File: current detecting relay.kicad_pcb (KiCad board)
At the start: 2 copper layers, 13 x 20.5 mm, 18 parts, among them J30 197054003, J85 197054101, J86 197054101, J87 197054003, Q1 SPP18P06P H, U1 INA300, U2 ULN2001D, U3 ADP7182AUJZ-5.0

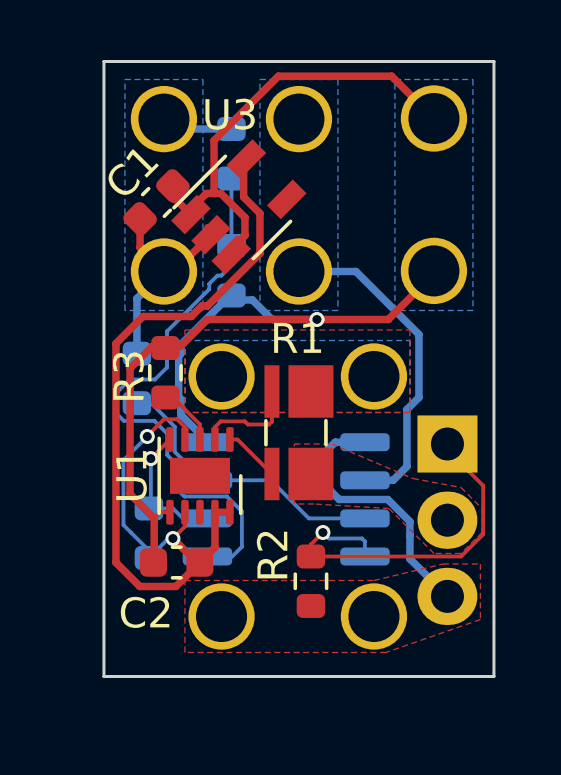
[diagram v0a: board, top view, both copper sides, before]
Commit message: Selected smaller transistors, layout tentative
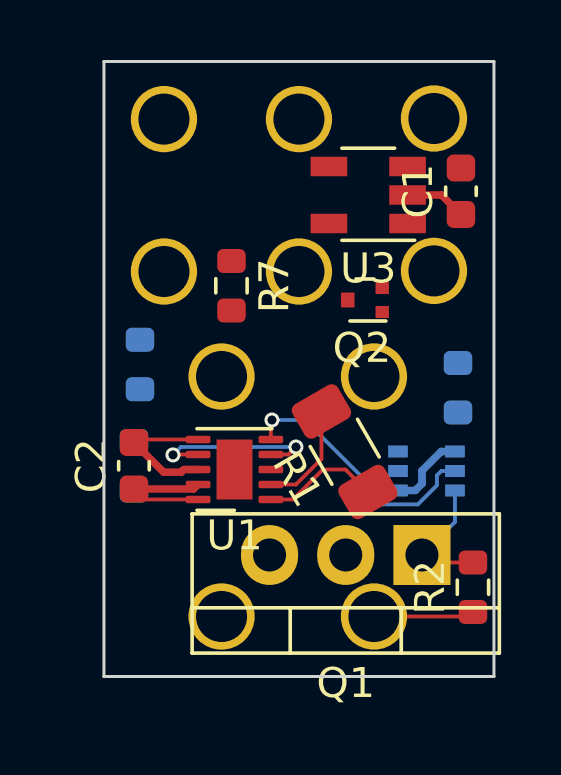
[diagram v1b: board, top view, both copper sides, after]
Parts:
- removed R6: 10K, Resistor_SMD:R_0603_1608Metric
- removed U2: ULN2001D, Package_SO:SOP-8_3.9x4.9mm_P1.27mm
- added Q2: Q_NPN_BEC, Package_TO_SOT_SMD:SOT-723, F.Cu at (108.7, 58.0)
- added Q3: BC846BDW1, Package_TO_SOT_SMD:SOT-363_SC-70-6, B.Cu at (110.8, 63.6)
- R1: footprint Resistor_SMD:R_Shunt_Ohmite_LVK12 -> Resistor_SMD:R_1206_3216Metric_Pad1.30x1.75mm_HandSolder
- R3: moved to B.Cu
- R7: moved to F.Cu
- moved R4 11.4 mm to (111.8, 60.9), turned to 270 degrees
- moved C1 10.2 mm to (111.9, 54.3), turned to 90 degrees
- moved R5 7.66 mm to (101.2, 60.1)
- moved R2 5.40 mm to (112.3, 67.5)
- moved R7 4.41 mm to (104.2, 57.5)
- moved U3 4.33 mm to (108.8, 54.5), turned to 180 degrees
- moved Q1 3.80 mm to (110.6, 66.5), turned to 180 degrees
- moved C2 3.53 mm to (101.0, 63.5), turned to 90 degrees
- moved R3 3.27 mm to (101.0, 63.5)
- moved R1 1.74 mm to (108.0, 63.0), turned to 120 degrees
- moved U1 1.17 mm to (104.3, 63.6), turned to 180 degrees
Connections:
- net Net-(R3-Pad2) renamed /LimSet
- J87 pad 1_1: /Vout -> /SHUNT-
- J87 pad 1_2: /Vout -> /SHUNT-
- R1 pad 2: /Vsense+ -> /SHUNT-
- U1 pad 1: /Vsense+ -> /SHUNT+
- U1 pad 2: /Vsense- -> /SHUNT-
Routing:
- net GND: track 43.6 -> 7.46 mm, vias 1 -> 0
- net /5V: track 32.8 -> 10.5 mm
- net Net-(Q3-Pad5): track 18.8 -> 0.00 mm
- net /LAMP: track 11.0 -> 0.00 mm
- net Net-(Q2-Pad1): track 9.68 -> 0.00 mm
- net /OutEnable: track 12.5 -> 4.41 mm, vias 1 -> 0
- net /SWin: track 9.74 -> 2.05 mm
- net /Vin: track 8.97 -> 3.36 mm
- net /ALERT: track 4.68 -> 8.73 mm
- net /SHUNT+: track 0.19 -> 3.96 mm
- net /SHUNT-: track 0.00 -> 3.62 mm
- net /Vsense-: track 3.48 -> 0.00 mm
- net /LimSet: track 2.32 -> 0.00 mm
- net /Vsense+: track 1.88 -> 0.00 mm
- removed copper zone on B.Cu, net /LAMP
- removed copper zone on F.Cu, net /SHUNT+
- removed copper zone on B.Cu, net /SWin
- removed copper zone on F.Cu, net /Vin
- removed copper zone on B.Cu, net /Vout
- removed copper zone on F.Cu, net /Vout
- removed copper zone on B.Cu, net GND

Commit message: Worked on layout and cleaning up silk screen
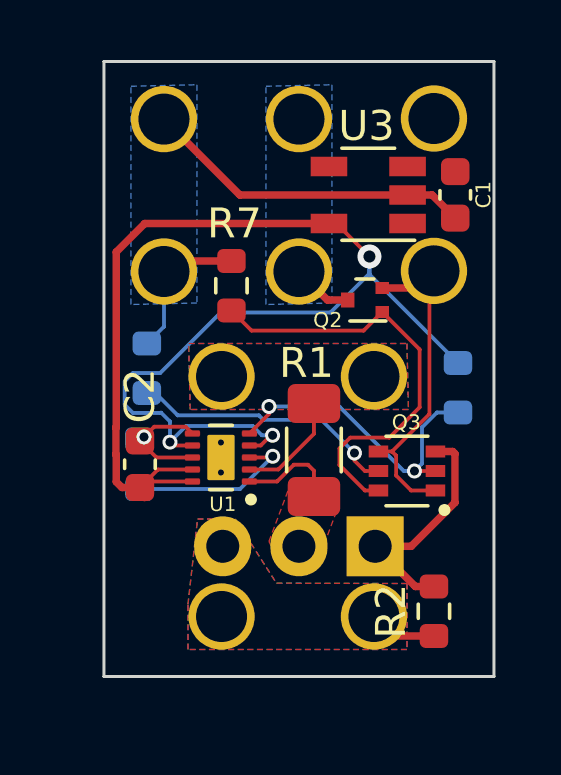
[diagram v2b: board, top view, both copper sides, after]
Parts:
- J30, J85, J86, J87, Ja87: moved to B.Cu
- Q3: moved to F.Cu
- U1: footprint Package_SON:WSON-10-1EP_2.5x2.5mm_P0.5mm_EP1.2x2mm -> footprints:SON40P200X200X80-11N
- moved Q1 1.59 mm to (109.0, 66.2)
- moved R2 1.53 mm to (111.0, 68.3)
- moved R1 1.03 mm to (107.0, 63.0), turned to 90 degrees
- moved Q3 0.65 mm to (110.1, 63.6)
- moved U1 0.60 mm to (103.9, 63.2)
- moved R5 0.26 mm to (101.4, 60.2)
- moved C1 0.22 mm to (111.7, 54.4)
- moved C2 0.21 mm to (101.2, 63.4)
- moved R3 0.19 mm to (101.2, 63.4)
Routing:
- net /5V: track 10.5 -> 45.9 mm, vias 2 -> 3
- net Net-(Q2-Pad1): track 0.00 -> 14.7 mm
- net /SWin: track 2.05 -> 15.9 mm
- net Net-(Q3-Pad5): track 0.00 -> 8.73 mm, vias 0 -> 1
- net GND: track 7.46 -> 15.6 mm, vias 0 -> 1
- net /LimSet: track 0.00 -> 5.69 mm, vias 0 -> 1
- net /OutEnable: track 4.41 -> 8.09 mm
- net /ALERT: track 8.73 -> 10.9 mm, vias 1 -> 2
- net /LAMP: track 0.00 -> 2.02 mm
- net /Vin: track 3.36 -> 2.27 mm
- net /SHUNT+: track 3.96 -> 3.42 mm
- added copper zone on B.Cu, net /LAMP
- added copper zone on F.Cu, net /SHUNT+
- added copper zone on B.Cu, net /SHUNT-
- added copper zone on F.Cu, net /SHUNT-
- added copper zone on B.Cu, net /SWin
- added copper zone on B.Cu, net /Vin
- added copper zone on F.Cu, net /Vin
- added copper zone on B.Cu, net GND
- added copper zone on F.Cu, net GND
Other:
- board text added: "CURRENT DETECTING RELAY V1.0"
- board text added: "github.com/grahamjr/ current-sense-relay"

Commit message: Upgraded to kicad V9
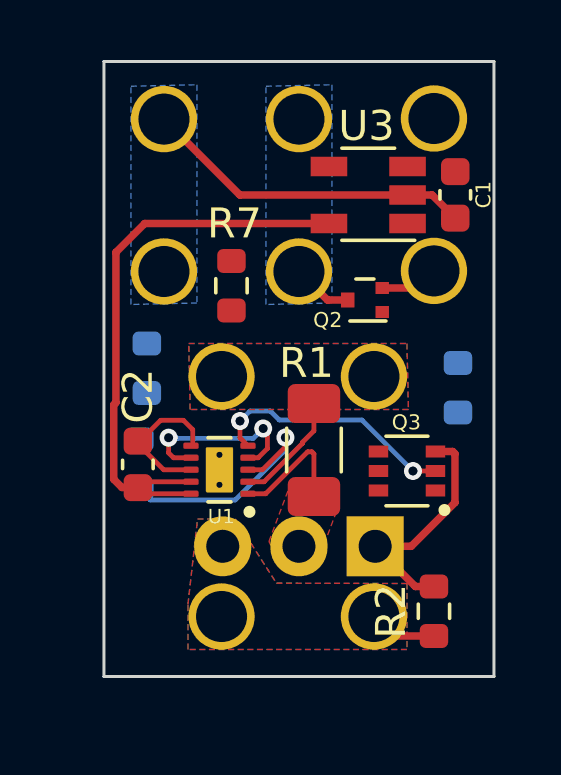
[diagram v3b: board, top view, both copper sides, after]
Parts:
- moved U1 0.41 mm to (103.8, 63.6)
- moved C2 0.07 mm to (101.1, 63.4)
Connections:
- U3 pad 4: (no net) -> unconnected-(U3-NC-Pad4)
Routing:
- net /5V: track 45.9 -> 26.2 mm, vias 3 -> 2
- net Net-(Q2-B): track 14.7 -> 0.00 mm
- net Net-(Q3B-B2): track 8.73 -> 0.00 mm, vias 1 -> 0
- net GND: track 15.6 -> 7.23 mm, vias 1 -> 0
- net /SWin: track 15.9 -> 11.1 mm
- net /ALERT: track 10.9 -> 8.42 mm
- net /LimSet: track 5.69 -> 8.00 mm
- net /SHUNT+: track 3.42 -> 4.17 mm
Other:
- net class Default removed
- net class Pwr removed
